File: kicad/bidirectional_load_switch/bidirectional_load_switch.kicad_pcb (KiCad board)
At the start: 2 copper layers, 452.1 x 259 mm, 156 parts, among them J101 1017503, J102 Conn_01x09_Socket, J103 Conn_01x02_Socket, J104 Conn_01x02_Socket, J105 Conn_01x02_Socket, J106 Conn_01x02_Socket, J107 AVR-ISP-6, SW101 PTS526 SK15 SMTR2 LFS, U101 TMCS1101A3BQDR, U102 TLV75733PDBVR, U104 ATTINY85-20SU, U201 SN74LVC1G17DCKR, U202 UCC23313DWYR, U203 SISS94DN-T1-GE3, U204 SISS94DN-T1-GE3, U205 SN74LVC1G08DCKR, U301 SN74LVC1G17DCKR, U302 UCC23313DWYR, U303 SISS94DN-T1-GE3, U304 SISS94DN-T1-GE3, U305 SN74LVC1G08DCKR, U401 SN74LVC1G17DCKR, U402 UCC23313DWYR, U403 SISS94DN-T1-GE3, U404 SISS94DN-T1-GE3, U405 SN74LVC1G08DCKR, U501 SN74LVC1G17DCKR, U502 UCC23313DWYR, U503 SISS94DN-T1-GE3, U504 SISS94DN-T1-GE3, U505 SN74LVC1G08DCKR, U601 SN74LVC1G17DCKR, U602 UCC23313DWYR, U603 SISS94DN-T1-GE3, U604 SISS94DN-T1-GE3, U605 SN74LVC1G08DCKR, U701 SN74LVC1G17DCKR, U702 UCC23313DWYR, U703 SISS94DN-T1-GE3, U704 SISS94DN-T1-GE3, U705 SN74LVC1G08DCKR, U801 SN74LVC1G17DCKR, U802 UCC23313DWYR, U803 SISS94DN-T1-GE3, U804 SISS94DN-T1-GE3, U805 SN74LVC1G08DCKR, U901 SN74LVC1G17DCKR, U902 UCC23313DWYR, U903 SISS94DN-T1-GE3, U904 SISS94DN-T1-GE3, U905 SN74LVC1G08DCKR

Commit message: almost
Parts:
- removed C108, C109: 100n, Capacitor_SMD:C_0603_1608Metric
- removed U104: ATTINY85-20SU, mcu_ATTINY85_20SU:8S2_ATM
- added C102: 10u, Capacitor_SMD:C_1206_3216Metric, F.Cu at (146.1, 12.4)
- added C103: 100n, Capacitor_SMD:C_0603_1608Metric, F.Cu at (66.6, 49.7)
- added D101: CUS10S30_H3F, diode_CUS10S30_H3F:USC_TOS, F.Cu at (191.2, 36.2)
- added U103: ATTINY85-20SU, mcu_ATTINY85_20SU:8S2_ATM, F.Cu at (130.0, 21.5)
- C104, C204, C304, C404, C504, C604, C704, C804, C904: value 100n -> 10u; footprint Capacitor_SMD:C_0603_1608Metric -> Capacitor_SMD:C_1206_3216Metric
- C106, C107, C203, C303, C403, C503, C603, C703, C803, C903: value 10u -> 100n; footprint Capacitor_SMD:C_1206_3216Metric -> Capacitor_SMD:C_0603_1608Metric
- C201, C301, C401, C501, C601, C701, C801, C901: value 1u -> 100n
- C202, C302, C402, C502, C602, C702, C802, C902: value 100n -> 1u
- J102: value Conn_01x09_Socket -> Conn_01x02_Socket; footprint Connector_PinHeader_2.54mm:PinHeader_1x09_P2.54mm_Vertical -> Connector_PinHeader_2.54mm:PinHeader_1x02_P2.54mm_Vertical
- J103: value Conn_01x02_Socket -> Conn_01x09_Socket; footprint Connector_PinHeader_2.54mm:PinHeader_1x02_P2.54mm_Vertical -> Connector_PinHeader_2.54mm:PinHeader_1x09_P2.54mm_Vertical
- U102: footprint ldo_TLV75733PDBVR:DBV0005A_N -> ldo_TLV75733PDBVR:DBV0005A_L
- U201, U301, U401, U501, U601, U701, U801, U901: value SN74LVC1G17DCKR -> SN74LVC1G08DCKR; footprint buffer_SN74LVC1G17DCKR:DCK5 -> and_gate_SN74LVC1G08DCKR:DCK5
- U202, U302, U402, U502, U602, U702, U802, U902: value UCC23313DWYR -> SN74LVC1G17DCKR; footprint gate_driver_UCC23313DWYR:SOIC6_DWY_TEX -> buffer_SN74LVC1G17DCKR:DCK5
- U203, U303, U403, U503, U603, U703, U803, U903: value SISS94DN-T1-GE3 -> UCC23313DWYR; footprint mosfet_SISS94DN-T1-GE3:MOSFET_3DN-T1-GE3_VIS -> gate_driver_UCC23313DWYR:SOIC6_DWY_TEX
- U204, U304, U404, U504, U604, U704, U804, U904: value SISS94DN-T1-GE3 -> STD16N60M6; footprint mosfet_SISS94DN-T1-GE3:MOSFET_3DN-T1-GE3_VIS -> mosfet_STD16N60M6:DPAKTO-252_STM
- U205, U305, U405, U505, U605, U705, U805, U905: value SN74LVC1G08DCKR -> STD16N60M6; footprint and_gate_SN74LVC1G08DCKR:DCK5 -> mosfet_STD16N60M6:DPAKTO-252_STM
- moved U904 139.7 mm to (4.30, 95.6), turned to 0 degrees
- moved U804 131.0 mm to (14.2, 80.9), turned to 0 degrees
- moved U604 124.6 mm to (4.30, 110.3), turned to 0 degrees
- moved U704 124.6 mm to (4.30, 125.0), turned to 0 degrees
- moved U205 124.2 mm to (218.5, 56.2), turned to -90 degrees
- moved U304 119.4 mm to (22.1, 125.0), turned to 0 degrees
- moved RS108 116.5 mm to (43.1, 82.6), turned to 0 degrees
- moved RS107 110.9 mm to (43.1, 77.8), turned to 0 degrees
- moved U404 109.4 mm to (22.1, 110.3), turned to 0 degrees
- moved C901 109.2 mm to (84.6, 47.2), turned to 0 degrees
- moved R904 108.9 mm to (105.3, 47.4)
- moved C205 108.5 mm to (205.8, 50.2)
- moved R905 107.9 mm to (105.3, 50.4)
- moved C902 107.0 mm to (84.6, 49.7), turned to 0 degrees
- moved U504 106.8 mm to (22.1, 95.6), turned to 0 degrees
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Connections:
- C101 pad 1: 3V3 -> 5V
- C105 pad 1: 5V -> 3V3
- C106 pad 1: 5V -> 3V3
- C107 pad 1: 3V3 -> ~{MCU_RST}
- C203 pad 1: 15V_isolated -> 3V3
- C203 pad 2: GNDPWR -> GND
- C205 pad 1: 3V3 -> 15V_isolated
- C205 pad 2: GND -> GNDPWR
- C303 pad 1: 15V_isolated -> 3V3
- C303 pad 2: GNDPWR -> GND
- C305 pad 1: 3V3 -> 15V_isolated
- C305 pad 2: GND -> GNDPWR
- C403 pad 1: 15V_isolated -> 3V3
- C403 pad 2: GNDPWR -> GND
- C405 pad 1: 3V3 -> 15V_isolated
- C405 pad 2: GND -> GNDPWR
- C503 pad 1: 15V_isolated -> 3V3
- C503 pad 2: GNDPWR -> GND
- C505 pad 1: 3V3 -> 15V_isolated
- C505 pad 2: GND -> GNDPWR
- C603 pad 1: 15V_isolated -> 3V3
- C603 pad 2: GNDPWR -> GND
- C605 pad 1: 3V3 -> 15V_isolated
- C605 pad 2: GND -> GNDPWR
- C703 pad 1: 15V_isolated -> 3V3
- C703 pad 2: GNDPWR -> GND
- C705 pad 1: 3V3 -> 15V_isolated
- C705 pad 2: GND -> GNDPWR
- C803 pad 1: 15V_isolated -> 3V3
- C803 pad 2: GNDPWR -> GND
- C805 pad 1: 3V3 -> 15V_isolated
- C805 pad 2: GND -> GNDPWR
- C903 pad 1: 15V_isolated -> 3V3
- C903 pad 2: GNDPWR -> GND
- C905 pad 1: 3V3 -> 15V_isolated
- C905 pad 2: GND -> GNDPWR
- J102 pad 1: PWM1_in -> GND
- J102 pad 2: PWM2_in -> 5V
- J103 pad 1: GND -> PWM1_in
- J103 pad 2: 5V -> PWM2_in
- LED201 pad 2: Net-(U201-A) -> Net-(U201-Y)
- LED301 pad 2: Net-(U301-A) -> Net-(U301-Y)
- LED401 pad 2: Net-(U401-A) -> Net-(U401-Y)
- LED501 pad 2: Net-(U501-A) -> Net-(U501-Y)
- LED601 pad 2: Net-(U601-A) -> Net-(U601-Y)
- LED701 pad 2: Net-(U701-A) -> Net-(U701-Y)
- LED801 pad 2: Net-(U801-A) -> Net-(U801-Y)
- LED901 pad 2: Net-(U901-A) -> Net-(U901-Y)
- R202 pad 1: Net-(U201-Y) -> Net-(U202-Y)
- R202 pad 2: Net-(U202-ANODE) -> Net-(U203-ANODE)
- R203 pad 2: Net-(U202-CATHODE) -> Net-(U203-CATHODE)
- R204 pad 1: Net-(U202-VOUT) -> Net-(U203-VOUT)
- R204 pad 2: /Channel 1/VG1 -> Net-(R204-Pad2)
- R205 pad 1: Net-(U202-VOUT) -> Net-(U203-VOUT)
- R205 pad 2: /Channel 1/VG2 -> Net-(R205-Pad2)
- R302 pad 1: Net-(U301-Y) -> Net-(U302-Y)
- R302 pad 2: Net-(U302-ANODE) -> Net-(U303-ANODE)
- R303 pad 2: Net-(U302-CATHODE) -> Net-(U303-CATHODE)
- R304 pad 1: Net-(U302-VOUT) -> Net-(U303-VOUT)
- R304 pad 2: /Channel 2/VG1 -> Net-(R304-Pad2)
- R305 pad 1: Net-(U302-VOUT) -> Net-(U303-VOUT)
- R305 pad 2: /Channel 2/VG2 -> Net-(R305-Pad2)
- R402 pad 1: Net-(U401-Y) -> Net-(U402-Y)
- R402 pad 2: Net-(U402-ANODE) -> Net-(U403-ANODE)
- R403 pad 2: Net-(U402-CATHODE) -> Net-(U403-CATHODE)
- R404 pad 1: Net-(U402-VOUT) -> Net-(U403-VOUT)
- R404 pad 2: /Channel 3/VG1 -> Net-(R404-Pad2)
- R405 pad 1: Net-(U402-VOUT) -> Net-(U403-VOUT)
- R405 pad 2: /Channel 3/VG2 -> Net-(R405-Pad2)
- R502 pad 1: Net-(U501-Y) -> Net-(U502-Y)
- R502 pad 2: Net-(U502-ANODE) -> Net-(U503-ANODE)
- R503 pad 2: Net-(U502-CATHODE) -> Net-(U503-CATHODE)
- R504 pad 1: Net-(U502-VOUT) -> Net-(U503-VOUT)
- R504 pad 2: /Channel 4/VG1 -> Net-(R504-Pad2)
- R505 pad 1: Net-(U502-VOUT) -> Net-(U503-VOUT)
- R505 pad 2: /Channel 4/VG2 -> Net-(R505-Pad2)
- R602 pad 1: Net-(U601-Y) -> Net-(U602-Y)
- R602 pad 2: Net-(U602-ANODE) -> Net-(U603-ANODE)
- R603 pad 2: Net-(U602-CATHODE) -> Net-(U603-CATHODE)
- R604 pad 1: Net-(U602-VOUT) -> Net-(U603-VOUT)
- R604 pad 2: /Channel 5/VG1 -> Net-(R604-Pad2)
- R605 pad 1: Net-(U602-VOUT) -> Net-(U603-VOUT)
- R605 pad 2: /Channel 5/VG2 -> Net-(R605-Pad2)
- R702 pad 1: Net-(U701-Y) -> Net-(U702-Y)
- R702 pad 2: Net-(U702-ANODE) -> Net-(U703-ANODE)
- R703 pad 2: Net-(U702-CATHODE) -> Net-(U703-CATHODE)
- R704 pad 1: Net-(U702-VOUT) -> Net-(U703-VOUT)
- R704 pad 2: /Channel 6/VG1 -> Net-(R704-Pad2)
- R705 pad 1: Net-(U702-VOUT) -> Net-(U703-VOUT)
- R705 pad 2: /Channel 6/VG2 -> Net-(R705-Pad2)
- R802 pad 1: Net-(U801-Y) -> Net-(U802-Y)
- R802 pad 2: Net-(U802-ANODE) -> Net-(U803-ANODE)
- R803 pad 2: Net-(U802-CATHODE) -> Net-(U803-CATHODE)
- R804 pad 1: Net-(U802-VOUT) -> Net-(U803-VOUT)
- R804 pad 2: /Channel 7/VG1 -> Net-(R804-Pad2)
- R805 pad 1: Net-(U802-VOUT) -> Net-(U803-VOUT)
- R805 pad 2: /Channel 7/VG2 -> Net-(R805-Pad2)
- R902 pad 1: Net-(U901-Y) -> Net-(U902-Y)
- R902 pad 2: Net-(U902-ANODE) -> Net-(U903-ANODE)
- R903 pad 2: Net-(U902-CATHODE) -> Net-(U903-CATHODE)
- R904 pad 1: Net-(U902-VOUT) -> Net-(U903-VOUT)
- R904 pad 2: /Channel 8/VG1 -> Net-(R904-Pad2)
- R905 pad 1: Net-(U902-VOUT) -> Net-(U903-VOUT)
- R905 pad 2: /Channel 8/VG2 -> Net-(R905-Pad2)
- U201 pad 1: unconnected-(U201-NC-Pad1) -> PWM1_in
- U201 pad 2: Net-(U201-A) -> ~{fault}
- U202 pad 1: Net-(U202-ANODE) -> unconnected-(U202-NC-Pad1)
- U202 pad 2: unconnected-(U202-NC-Pad2) -> Net-(U201-Y)
- U202 pad 3: Net-(U202-CATHODE) -> GND
- U202 pad 4: GNDPWR -> Net-(U202-Y)
- U202 pad 5: Net-(U202-VOUT) -> 3V3
- U203 pad 1: GNDPWR -> Net-(U203-ANODE)
- U203 pad 2: GNDPWR -> unconnected-(U203-NC-Pad2)
- U203 pad 3: GNDPWR -> Net-(U203-CATHODE)
- U203 pad 4: /Channel 1/VG1 -> GNDPWR
- U203 pad 5: /Channel 1/RIN -> Net-(U203-VOUT)
- U204 pad 1: GNDPWR -> Net-(R204-Pad2)
- U204 pad 2: GNDPWR -> /Channel 1/RIN
- U205 pad 1: PWM1_in -> Net-(R205-Pad2)
- U205 pad 2: ~{fault} -> Earth
- U205 pad 3: GND -> GNDPWR
- U301 pad 1: unconnected-(U301-NC-Pad1) -> PWM2_in
- U301 pad 2: Net-(U301-A) -> ~{fault}
- U302 pad 1: Net-(U302-ANODE) -> unconnected-(U302-NC-Pad1)
- U302 pad 2: unconnected-(U302-NC-Pad2) -> Net-(U301-Y)
- U302 pad 3: Net-(U302-CATHODE) -> GND
- U302 pad 4: GNDPWR -> Net-(U302-Y)
- U302 pad 5: Net-(U302-VOUT) -> 3V3
- U303 pad 1: GNDPWR -> Net-(U303-ANODE)
- U303 pad 2: GNDPWR -> unconnected-(U303-NC-Pad2)
- U303 pad 3: GNDPWR -> Net-(U303-CATHODE)
- U303 pad 4: /Channel 2/VG1 -> GNDPWR
- U303 pad 5: /Channel 2/RIN -> Net-(U303-VOUT)
- U304 pad 1: GNDPWR -> Net-(R304-Pad2)
- U304 pad 2: GNDPWR -> /Channel 2/RIN
- U305 pad 1: PWM2_in -> Net-(R305-Pad2)
- U305 pad 2: ~{fault} -> Earth
- U305 pad 3: GND -> GNDPWR
- U401 pad 1: unconnected-(U401-NC-Pad1) -> PWM3_in
- U401 pad 2: Net-(U401-A) -> ~{fault}
- U402 pad 1: Net-(U402-ANODE) -> unconnected-(U402-NC-Pad1)
- U402 pad 2: unconnected-(U402-NC-Pad2) -> Net-(U401-Y)
- U402 pad 3: Net-(U402-CATHODE) -> GND
- U402 pad 4: GNDPWR -> Net-(U402-Y)
- U402 pad 5: Net-(U402-VOUT) -> 3V3
- U403 pad 1: GNDPWR -> Net-(U403-ANODE)
- U403 pad 2: GNDPWR -> unconnected-(U403-NC-Pad2)
- U403 pad 3: GNDPWR -> Net-(U403-CATHODE)
- U403 pad 4: /Channel 3/VG1 -> GNDPWR
- U403 pad 5: /Channel 3/RIN -> Net-(U403-VOUT)
- U404 pad 1: GNDPWR -> Net-(R404-Pad2)
- U404 pad 2: GNDPWR -> /Channel 3/RIN
- U405 pad 1: PWM3_in -> Net-(R405-Pad2)
- U405 pad 2: ~{fault} -> Earth
- U405 pad 3: GND -> GNDPWR
- U501 pad 1: unconnected-(U501-NC-Pad1) -> PWM4_in
- U501 pad 2: Net-(U501-A) -> ~{fault}
- U502 pad 1: Net-(U502-ANODE) -> unconnected-(U502-NC-Pad1)
- U502 pad 2: unconnected-(U502-NC-Pad2) -> Net-(U501-Y)
- U502 pad 3: Net-(U502-CATHODE) -> GND
- U502 pad 4: GNDPWR -> Net-(U502-Y)
- U502 pad 5: Net-(U502-VOUT) -> 3V3
- U503 pad 1: GNDPWR -> Net-(U503-ANODE)
- U503 pad 2: GNDPWR -> unconnected-(U503-NC-Pad2)
- U503 pad 3: GNDPWR -> Net-(U503-CATHODE)
- U503 pad 4: /Channel 4/VG1 -> GNDPWR
- U503 pad 5: /Channel 4/RIN -> Net-(U503-VOUT)
- U504 pad 1: GNDPWR -> Net-(R504-Pad2)
- U504 pad 2: GNDPWR -> /Channel 4/RIN
- U505 pad 1: PWM4_in -> Net-(R505-Pad2)
- U505 pad 2: ~{fault} -> Earth
- U505 pad 3: GND -> GNDPWR
- U601 pad 1: unconnected-(U601-NC-Pad1) -> PWM5_in
- U601 pad 2: Net-(U601-A) -> ~{fault}
- U602 pad 1: Net-(U602-ANODE) -> unconnected-(U602-NC-Pad1)
- U602 pad 2: unconnected-(U602-NC-Pad2) -> Net-(U601-Y)
- U602 pad 3: Net-(U602-CATHODE) -> GND
- U602 pad 4: GNDPWR -> Net-(U602-Y)
- U602 pad 5: Net-(U602-VOUT) -> 3V3
- U603 pad 1: GNDPWR -> Net-(U603-ANODE)
- U603 pad 2: GNDPWR -> unconnected-(U603-NC-Pad2)
- U603 pad 3: GNDPWR -> Net-(U603-CATHODE)
- U603 pad 4: /Channel 5/VG1 -> GNDPWR
- U603 pad 5: /Channel 5/RIN -> Net-(U603-VOUT)
- U604 pad 1: GNDPWR -> Net-(R604-Pad2)
- U604 pad 2: GNDPWR -> /Channel 5/RIN
- U605 pad 1: PWM5_in -> Net-(R605-Pad2)
- U605 pad 2: ~{fault} -> Earth
- U605 pad 3: GND -> GNDPWR
- U701 pad 1: unconnected-(U701-NC-Pad1) -> PWM6_in
- U701 pad 2: Net-(U701-A) -> ~{fault}
- U702 pad 1: Net-(U702-ANODE) -> unconnected-(U702-NC-Pad1)
- U702 pad 2: unconnected-(U702-NC-Pad2) -> Net-(U701-Y)
- U702 pad 3: Net-(U702-CATHODE) -> GND
- U702 pad 4: GNDPWR -> Net-(U702-Y)
- U702 pad 5: Net-(U702-VOUT) -> 3V3
- U703 pad 1: GNDPWR -> Net-(U703-ANODE)
- U703 pad 2: GNDPWR -> unconnected-(U703-NC-Pad2)
- U703 pad 3: GNDPWR -> Net-(U703-CATHODE)
- U703 pad 4: /Channel 6/VG1 -> GNDPWR
- U703 pad 5: /Channel 6/RIN -> Net-(U703-VOUT)
- U704 pad 1: GNDPWR -> Net-(R704-Pad2)
- U704 pad 2: GNDPWR -> /Channel 6/RIN
- U705 pad 1: PWM6_in -> Net-(R705-Pad2)
- U705 pad 2: ~{fault} -> Earth
- U705 pad 3: GND -> GNDPWR
- U801 pad 1: unconnected-(U801-NC-Pad1) -> PWM7_in
- U801 pad 2: Net-(U801-A) -> ~{fault}
- U802 pad 1: Net-(U802-ANODE) -> unconnected-(U802-NC-Pad1)
- U802 pad 2: unconnected-(U802-NC-Pad2) -> Net-(U801-Y)
- U802 pad 3: Net-(U802-CATHODE) -> GND
- U802 pad 4: GNDPWR -> Net-(U802-Y)
- U802 pad 5: Net-(U802-VOUT) -> 3V3
- U803 pad 1: GNDPWR -> Net-(U803-ANODE)
- U803 pad 2: GNDPWR -> unconnected-(U803-NC-Pad2)
- U803 pad 3: GNDPWR -> Net-(U803-CATHODE)
- U803 pad 4: /Channel 7/VG1 -> GNDPWR
- U803 pad 5: /Channel 7/RIN -> Net-(U803-VOUT)
- U804 pad 1: GNDPWR -> Net-(R804-Pad2)
- U804 pad 2: GNDPWR -> /Channel 7/RIN
- U805 pad 1: PWM7_in -> Net-(R805-Pad2)
- U805 pad 2: ~{fault} -> Earth
- U805 pad 3: GND -> GNDPWR
- U901 pad 1: unconnected-(U901-NC-Pad1) -> PWM8_in
- U901 pad 2: Net-(U901-A) -> ~{fault}
- U902 pad 1: Net-(U902-ANODE) -> unconnected-(U902-NC-Pad1)
- U902 pad 2: unconnected-(U902-NC-Pad2) -> Net-(U901-Y)
- U902 pad 3: Net-(U902-CATHODE) -> GND
- U902 pad 4: GNDPWR -> Net-(U902-Y)
- U902 pad 5: Net-(U902-VOUT) -> 3V3
- U903 pad 1: GNDPWR -> Net-(U903-ANODE)
- U903 pad 2: GNDPWR -> unconnected-(U903-NC-Pad2)
- U903 pad 3: GNDPWR -> Net-(U903-CATHODE)
- U903 pad 4: /Channel 8/VG1 -> GNDPWR
- U903 pad 5: /Channel 8/RIN -> Net-(U903-VOUT)
- U904 pad 1: GNDPWR -> Net-(R904-Pad2)
- U904 pad 2: GNDPWR -> /Channel 8/RIN
- U905 pad 1: PWM8_in -> Net-(R905-Pad2)
- U905 pad 2: ~{fault} -> Earth
- U905 pad 3: GND -> GNDPWR
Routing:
- net 3V3: track 141.5 -> 0.00 mm, vias 0 -> 4
- net Net-(U201-Y): track 1.80 -> 4.99 mm
- net Net-(U203-ANODE): track 0.00 -> 2.70 mm
- net Net-(U202-Y): track 0.00 -> 2.49 mm
- net Net-(U203-CATHODE): track 0.00 -> 2.31 mm
- net Net-(U702-CATHODE): track 2.15 -> 0.00 mm
- net Net-(U302-CATHODE): track 2.15 -> 0.00 mm
- net Net-(U202-CATHODE): track 2.15 -> 0.00 mm
- net Net-(U602-CATHODE): track 2.15 -> 0.00 mm
- net Net-(U502-CATHODE): track 2.15 -> 0.00 mm
- net Net-(U402-CATHODE): track 2.15 -> 0.00 mm
- net Net-(U902-CATHODE): track 2.15 -> 0.00 mm
- net Net-(U802-CATHODE): track 2.15 -> 0.00 mm
- net Net-(U702-ANODE): track 2.14 -> 0.00 mm
- net Net-(U602-ANODE): track 2.14 -> 0.00 mm
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- added copper zone on B.Cu, net 3V3
- added copper zone on F.Cu, net 3V3
- added copper zone on F.Cu, net Net-(R204-Pad2)
- added copper zone on F.Cu, net Net-(R205-Pad2)
- added copper zone on F.Cu, net Net-(U203-VOUT)
- removed copper zone on F.Cu, net /Channel 1/VG1
- removed copper zone on F.Cu, net /Channel 1/VG2
- removed copper zone on F.Cu, net /Channel 2/RIN
- removed copper zone on F.Cu, net /Channel 2/VG1
- removed copper zone on F.Cu, net /Channel 2/VG2
- removed copper zone on F.Cu, net /Channel 3/RIN
- removed copper zone on F.Cu, net /Channel 3/VG1
- removed copper zone on F.Cu, net /Channel 3/VG2
- removed copper zone on F.Cu, net /Channel 4/RIN
- removed copper zone on F.Cu, net /Channel 4/VG1
- removed copper zone on F.Cu, net /Channel 4/VG2
- removed copper zone on F.Cu, net /Channel 5/RIN
- removed copper zone on F.Cu, net /Channel 5/VG1
- removed copper zone on F.Cu, net /Channel 5/VG2
- removed copper zone on F.Cu, net /Channel 6/RIN
- removed copper zone on F.Cu, net /Channel 6/VG1
- removed copper zone on F.Cu, net /Channel 6/VG2
- removed copper zone on F.Cu, net /Channel 7/RIN
- removed copper zone on F.Cu, net /Channel 7/VG1
- removed copper zone on F.Cu, net /Channel 7/VG2
- removed copper zone on F.Cu, net /Channel 8/RIN
- removed copper zone on F.Cu, net /Channel 8/VG1
- removed copper zone on F.Cu, net /Channel 8/VG2
- removed copper zone on F.Cu, net 15V_isolated
- removed copper zone on F.Cu, net Net-(U202-VOUT)
- removed copper zone on F.Cu, net Net-(U302-VOUT)
- removed copper zone on F.Cu, net Net-(U402-VOUT)
- removed copper zone on F.Cu, net Net-(U502-VOUT)
- removed copper zone on F.Cu, net Net-(U602-VOUT)
- removed copper zone on F.Cu, net Net-(U702-VOUT)
- removed copper zone on F.Cu, net Net-(U802-VOUT)
- removed copper zone on F.Cu, net Net-(U902-VOUT)
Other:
- board size 452.1 x 259 mm -> 263.1 x 151.5 mm
- rule pad_to_mask_clearance: 0.0508 -> 0.038
- board text removed: "0.1524 mm / 0.1524 mm"
- board text removed: "0.2540 mm"
- board text removed: "1.6000 mm"
- board text removed: "2"
- board text removed: "55.6500 mm x 126.5000 mm"
- board text removed: "BOARD CHARACTERISTICS"
- board text removed: "Board Thickness:"
- board text removed: "Board overall dimensions:"
- board text removed: "Castellated pads:"
- board text removed: "Copper Finish:"
- board text removed: "Copper Layer Count:"
- board text removed: "ENIG"
- board text removed: "Edge card connectors:"
- board text removed: "Impedance Control:"
- board text removed: "Min hole diameter:"
- board text removed: "Min track/spacing:"
- board text removed: "No"
- board text removed: "Plated Board Edge:"

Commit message: needs review
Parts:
- added C206: 100n, Capacitor_SMD:C_0603_1608Metric, F.Cu at (95.8, 96.8)
- added C306: 100n, Capacitor_SMD:C_0603_1608Metric, F.Cu at (114.3, 96.8)
- added C406: 100n, Capacitor_SMD:C_0603_1608Metric, F.Cu at (132.8, 96.8)
- added C506: 100n, Capacitor_SMD:C_0603_1608Metric, F.Cu at (151.3, 96.8)
- added C606: 100n, Capacitor_SMD:C_0603_1608Metric, F.Cu at (169.8, 96.8)
- added C706: 100n, Capacitor_SMD:C_0603_1608Metric, F.Cu at (188.3, 96.8)
- added C806: 100n, Capacitor_SMD:C_0603_1608Metric, F.Cu at (206.8, 96.8)
- added C906: 100n, Capacitor_SMD:C_0603_1608Metric, F.Cu at (225.3, 96.8)
- C201, C203, C301, C303, C401, C403, C501, C503, C601, C603, C701, C703, C801, C803, C901, C903: value 100n -> 1u
- C202, C302, C402, C502, C602, C702, C802, C902: value 1u -> 100n
- C204, C304, C404, C504, C604, C704, C804, C904: value 10u -> 100n; footprint Capacitor_SMD:C_1206_3216Metric -> Capacitor_SMD:C_0603_1608Metric
- C205, C305, C405, C505, C605, C705, C805, C905: value 100n -> 10u; footprint Capacitor_SMD:C_0603_1608Metric -> Capacitor_SMD:C_1206_3216Metric
- R101: value 10k -> 150
- SW101: footprint switch_switch_PTS526_SK15_SMTR2_LFS:SMT_FS -> switch_PTS526_SK15_SMTR2_LFS:SMT_FS
- U101: value TMCS1101A3BQDR -> TMCS1101A3BQDRQ1
- moved U905 219.5 mm to (231.3, 84.1)
- moved U904 218.1 mm to (222.1, 84.2)
- moved U805 190.8 mm to (212.8, 84.1)
- moved U804 189.4 mm to (203.6, 84.2)
- moved U705 186.7 mm to (194.3, 84.1)
- moved U704 185.4 mm to (185.1, 84.2)
- moved RS108 179.7 mm to (222.1, 66.6), turned to -90 degrees
- moved U605 165.7 mm to (175.8, 84.1)
- moved U604 164.4 mm to (166.6, 84.2)
- moved RS107 160.9 mm to (203.6, 66.6), turned to -90 degrees
- moved R901 155.3 mm to (228.6, 115.3), turned to 90 degrees
- moved C901 155.2 mm to (221.6, 120.1), turned to 180 degrees
- moved J101 153.4 mm to (88.3, 63.1), turned to 180 degrees
- moved C902 153.1 mm to (221.6, 118.1), turned to 180 degrees
- moved R801 152.4 mm to (210.1, 115.3), turned to 90 degrees
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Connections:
- C204 pad 1: 15V_isolated -> 3V3
- C204 pad 2: GNDPWR -> GND
- C304 pad 1: 15V_isolated -> 3V3
- C304 pad 2: GNDPWR -> GND
- C404 pad 1: 15V_isolated -> 3V3
- C404 pad 2: GNDPWR -> GND
- C504 pad 1: 15V_isolated -> 3V3
- C504 pad 2: GNDPWR -> GND
- C604 pad 1: 15V_isolated -> 3V3
- C604 pad 2: GNDPWR -> GND
- C704 pad 1: 15V_isolated -> 3V3
- C704 pad 2: GNDPWR -> GND
- C804 pad 1: 15V_isolated -> 3V3
- C804 pad 2: GNDPWR -> GND
- C904 pad 1: 15V_isolated -> 3V3
- C904 pad 2: GNDPWR -> GND
- U101 pad 1: AC_post_sense -> AC_in
- U101 pad 2: AC_post_sense -> AC_in
- U101 pad 3: AC_in -> AC_post_sense
- U101 pad 4: AC_in -> AC_post_sense
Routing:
- net ~{fault}: track 0.00 -> 173.7 mm
- net PWM8_in: track 0.00 -> 160.3 mm
- net PWM7_in: track 0.00 -> 139.0 mm
- net PWM6_in: track 0.00 -> 117.7 mm
- net 3V3: track 0.00 -> 104.4 mm, vias 4 -> 44
- net PWM5_in: track 0.00 -> 96.3 mm
- net PWM4_in: track 0.00 -> 75.0 mm
- net PWM3_in: track 0.00 -> 53.7 mm
- net ~{MCU_RST}: track 0.00 -> 41.7 mm, vias 0 -> 2
- net SCK/~{fault_rst}: track 0.00 -> 33.6 mm
- net PWM2_in: track 0.00 -> 32.3 mm
- net MOSI: track 0.00 -> 25.5 mm
- net MISO/fault_status: track 0.00 -> 22.4 mm
- net GND: track 0.00 -> 19.8 mm, vias 6 -> 65
- net PWM1_in: track 0.00 -> 10.4 mm
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- added copper zone on F.Cu, net /Channel 2/RIN
- added copper zone on F.Cu, net /Channel 3/RIN
- added copper zone on F.Cu, net /Channel 4/RIN
- added copper zone on F.Cu, net /Channel 5/RIN
- added copper zone on F.Cu, net /Channel 6/RIN
- added copper zone on F.Cu, net /Channel 7/RIN
- added copper zone on F.Cu, net /Channel 8/RIN
- added copper zone on F.Cu, net 15V_isolated
- added copper zone on F.Cu, net 5V
- added copper zone on F.Cu, net Net-(R304-Pad2)
- added copper zone on F.Cu, net Net-(R305-Pad2)
- added copper zone on F.Cu, net Net-(R404-Pad2)
- added copper zone on F.Cu, net Net-(R405-Pad2)
- added copper zone on F.Cu, net Net-(R504-Pad2)
- added copper zone on F.Cu, net Net-(R505-Pad2)
- added copper zone on F.Cu, net Net-(R604-Pad2)
- added copper zone on F.Cu, net Net-(R605-Pad2)
- added copper zone on F.Cu, net Net-(R704-Pad2)
- added copper zone on F.Cu, net Net-(R705-Pad2)
- added copper zone on F.Cu, net Net-(R804-Pad2)
- added copper zone on F.Cu, net Net-(R805-Pad2)
- added copper zone on F.Cu, net Net-(R904-Pad2)
- added copper zone on F.Cu, net Net-(R905-Pad2)
- added copper zone on F.Cu, net Net-(U303-VOUT)
- added copper zone on F.Cu, net Net-(U403-VOUT)
- added copper zone on F.Cu, net Net-(U503-VOUT)
- added copper zone on F.Cu, net Net-(U603-VOUT)
- added copper zone on F.Cu, net Net-(U703-VOUT)
- added copper zone on F.Cu, net Net-(U803-VOUT)
- added copper zone on F.Cu, net Net-(U903-VOUT)
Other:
- board size 263.1 x 151.5 mm -> 176.8 x 67.3 mm

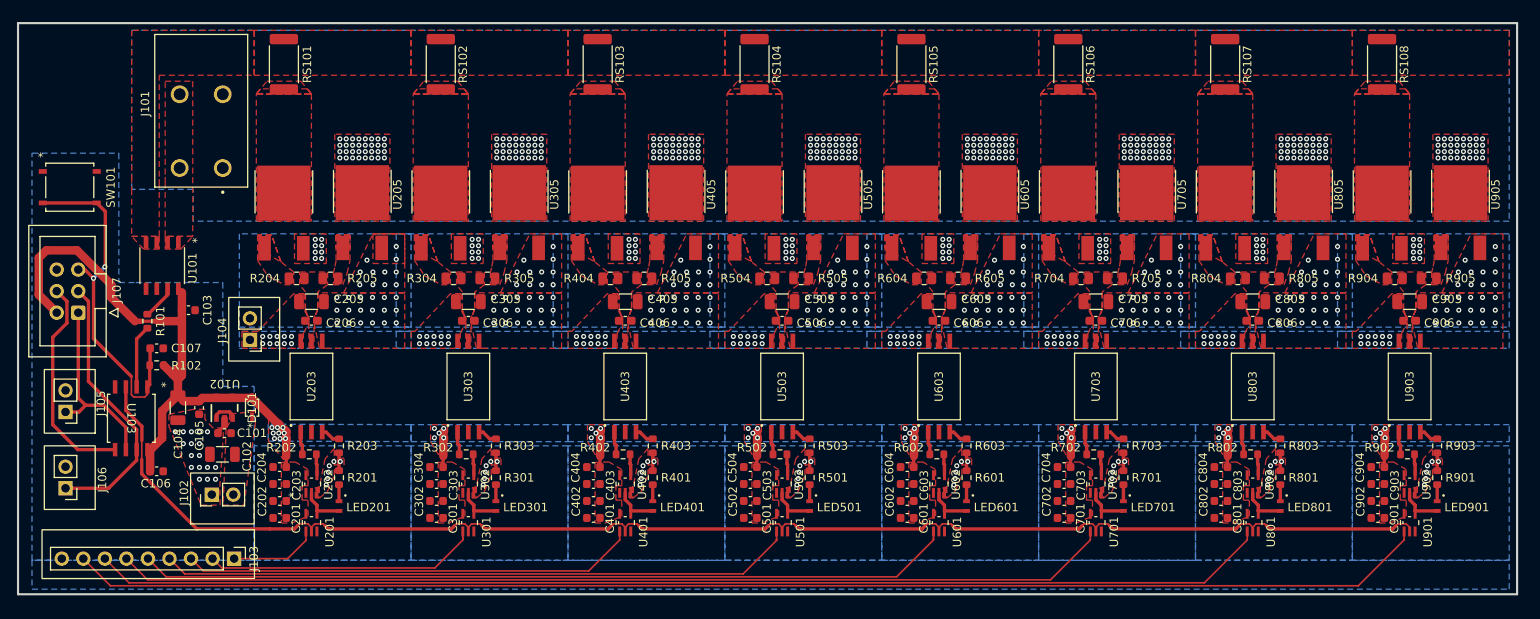
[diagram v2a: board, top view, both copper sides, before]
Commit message: updated layout and silkscreen
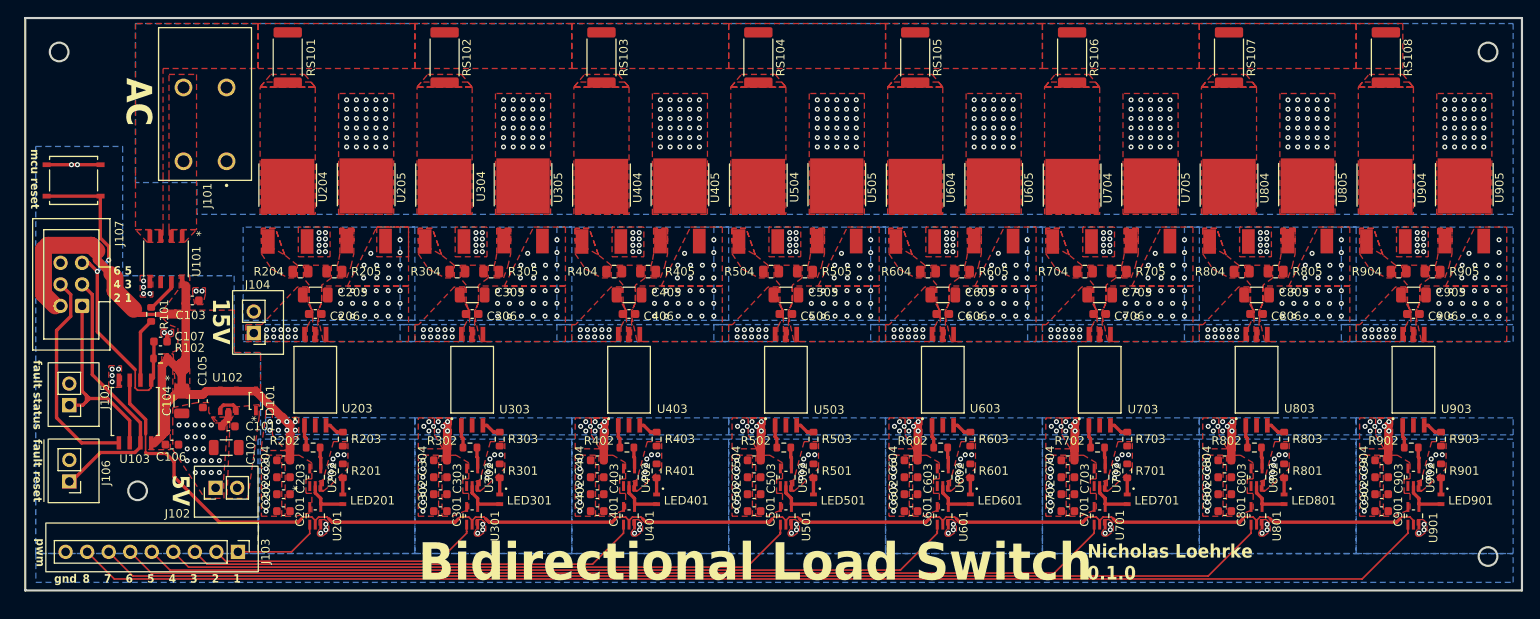
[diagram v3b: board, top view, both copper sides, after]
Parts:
- moved C106 3.63 mm to (79.4, 111.5)
- moved C103 1.23 mm to (81.8, 94.5)
- moved U102 0.94 mm to (86.1, 106.3)
- moved U401 0.92 mm to (133.3, 119.8)
- moved U404 0.92 mm to (130.1, 83.3)
- moved U501 0.92 mm to (151.8, 119.8)
- moved U504 0.92 mm to (148.6, 83.3)
- moved U601 0.92 mm to (170.3, 119.8)
- moved U604 0.92 mm to (167.1, 83.3)
- moved U701 0.92 mm to (188.8, 119.8)
- moved U704 0.92 mm to (185.6, 83.3)
- moved U801 0.92 mm to (207.3, 119.8)
- moved U804 0.92 mm to (204.1, 83.3)
- moved U901 0.92 mm to (225.8, 119.8)
- moved U904 0.92 mm to (222.6, 83.3)
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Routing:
- net 3V3: track 104.4 -> 125.6 mm, vias 44 -> 71
- net GND: track 19.8 -> 10.9 mm, vias 65 -> 162
- net MISO/fault_status: track 22.4 -> 23.2 mm
- net Earth: vias 256 -> 240
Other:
- board size 176.8 x 67.3 mm -> 176.5 x 67.5 mm
- board text added: "1"
- board text added: "15V"
- board text added: "2"
- board text added: "3"
- board text added: "4"
- board text added: "5"
- board text added: "5V"
- board text added: "6"
- board text added: "6 5 4 3 2 1"
- board text added: "7"
- board text added: "8"
- board text added: "AC"
- board text added: "Bidirectional Load Switch"
- board text added: "Nicholas Loehrke 0.1.0"
- board text added: "fault status"
- board text added: "gnd"
- board text added: "mcu reset"
- board text added: "pwm"
- board text added: "~{fault reset}"

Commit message: generated gerbers
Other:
- rule pad_to_mask_clearance: 0.038 -> 0
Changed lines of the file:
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@@
 			(dielectric_constraints no)
 		)
-		(pad_to_mask_clearance 0.038)
-		(solder_mask_min_width 0.1)
+		(pad_to_mask_clearance 0)
 		(allow_soldermask_bridges_in_footprints no)
 		(pcbplotparams
-			(layerselection 0x00010fc_ffffffff)
+			(layerselection 0x00010f8_ffffffff)
 			(plot_on_all_layers_selection 0x0000000_00000000)
 			(disableapertmacros no)
@@
 		(fp_arc
 			(start 0.723714 -1.445998)
-			(mid 0.776937 -1.423889)
+			(mid 0.77694 -1.423891)
 			(end 0.799455 -1.37084)
 			(stroke
@@
 		(fp_arc
 			(start 0.799455 1.399868)
-			(mid 0.776925 1.452897)
+			(mid 0.776922 1.452894)
 			(end 0.723713 1.475)
 			(stroke

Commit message: ready for order
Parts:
- added D102: CUS10S30_H3F, diode_CUS10S30_H3F:USC_TOS, F.Cu at (74.2, 94.4)
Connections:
- J107 pad 2: 3V3 -> Net-(J107-VCC)
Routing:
- net 3V3: track 125.6 -> 103.0 mm
- net Net-(J107-VCC): track 0.00 -> 21.2 mm
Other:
- board text added: "+ -"

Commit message: updated gerbers
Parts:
- D101, D102: value CUS10S30_H3F -> ~
- J101: value 1017503 -> ~
- LED201, LED301, LED401, LED501, LED601, LED701, LED801, LED901: value B1911PG--20D000514U1930 -> ~
- R201, R301, R401, R501, R601, R701, R801, R901: value 150 -> 220
- SW101: value PTS526 SK15 SMTR2 LFS -> ~
- U101: value TMCS1101A3BQDRQ1 -> ~
- U102: value TLV75733PDBVR -> ~
- U103: value ATTINY85-20SU -> ~
- U201, U301, U401, U501, U601, U701, U801, U901: value SN74LVC1G08DCKR -> ~
- U202, U302, U402, U502, U602, U702, U802, U902: value SN74LVC1G17DCKR -> ~
- U203, U303, U403, U503, U603, U703, U803, U903: value UCC23313DWYR -> ~
- U204, U205, U304, U305, U404, U405, U504, U505, U604, U605, U704, U705, U804, U805, U904, U905: value STD16N60M6 -> ~
